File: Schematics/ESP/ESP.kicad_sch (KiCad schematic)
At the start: 28 parts, among them J1 Barrel_Jack, Q1 IRLB8721PBF, Q10 IRLML0030, Q11 IRLML0030, Q12 IRLML0030, Q13 IRLML0030, Q14 IRLML0030, Q2 IRLB8721PBF, Q3 IRLB8721PBF, Q4 IRLB8721PBF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

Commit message: small tweaks
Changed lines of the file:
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@@
+    (stroke (width 0) (type default))
+  )
+  (wire (pts (xy 199.39 114.3) (xy 199.39 107.95))
     (stroke (width 0) (type default))
   )
@@
     (stroke (width 0) (type default))
   )
+  (wire (pts (xy 200.66 35.56) (xy 200.66 43.18))
+    (stroke (width 0) (type default))
+  )
   (wire (pts (xy 95.25 106.68) (xy 95.25 123.19))
     (stroke (width 0) (type default))
@@
   )
   (wire (pts (xy 69.85 63.5) (xy 95.25 63.5))
+    (stroke (width 0) (type default))
+  )
+  (wire (pts (xy 229.87 120.65) (xy 233.68 120.65))
     (stroke (width 0) (type default))
   )
@@
     )
   )
+  (global_label "Regulated 5V" (shape output) (at 233.68 120.65 0) (fields_autoplaced)
+    (effects (font (size 1.27 1.27)) (justify left))
+    (property "Intersheetrefs" "${INTERSHEET_REFS}" (at 249.08 120.65 0)
+      (effects (font (size 1.27 1.27)) (justify left) hide)
+    )
+  )
+  (global_label "Regulated 5V" (shape input) (at 200.66 35.56 90) (fields_autoplaced)
+    (effects (font (size 1.27 1.27)) (justify left))
+    (property "Intersheetrefs" "${INTERSHEET_REFS}" (at 200.66 20.16 90)
+      (effects (font (size 1.27 1.27)) (justify left) hide)
+    )
+  )
   (global_label "P-" (shape input) (at 259.08 27.94 180) (fields_autoplaced)
     (effects (font (size 1.27 1.27)) (justify right))
@@
     )
   )
+  (global_label "Power Supply" (shape input) (at 199.39 107.95 90) (fields_autoplaced)
+    (effects (font (size 1.27 1.27)) (justify left))
+    (property "Intersheetrefs" "${INTERSHEET_REFS}" (at 199.3106 92.6555 90)
+      (effects (font (size 1.27 1.27)) (justify left) hide)
+    )
+  )

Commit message: Schematics
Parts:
- removed BT1, BT2, BT4: Battery_Cell, symbol Device:Battery_Cell
- removed Q1, Q2, Q3, Q4, Q7, Q8: IRLB8721PBF, Package_TO_SOT_THT:TO-220-3_Vertical, symbol Transistor_FET:IRLB8721PBF
- removed Q10, Q11, Q12, Q13, Q14, Q9: IRLML0030, Package_TO_SOT_SMD:SOT-23, symbol Transistor_FET:IRLML0030
- added R11, R9: 2.7k, Resistor_SMD:R_1206_3216Metric_Pad1.30x1.75mm_HandSolder, symbol Device:R
- added SW2: SW_Push, Button_Switch_SMD:SW_SPST_PTS645, symbol Switch:SW_Push
- added U8, U9: 74LVC1G11, Package_TO_SOT_SMD:SOT-23-6_Handsoldering, symbol 74xGxx:74LVC1G11
- C1, C2, C3: footprint (none) -> Capacitor_Tantalum_SMD:CP_EIA-7343-31_Kemet-D_Pad2.25x2.55mm_HandSolder
- J1: footprint (none) -> RAPC722X:SWITCHCRAFT_RAPC722X
- Q6: digikey link (none) -> https://www.digikey.fi/en/products/detail/infineon-technolo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
- R2, R3, R5, R6: footprint (none) -> Resistor_SMD:R_1206_3216Metric_Pad1.30x1.75mm_HandSolder
- U2: digikey link (none) -> https://www.digikey.fi/en/products/detail/diodes-incorporat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
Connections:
- net P-: now also Q5.3 (S), SW2.1; no longer Q6.3 (S), R5.1
- net at Q6.1 (G): now also U9.4
- net DO2: now reaches U1.4 (DO)
- net DO2: now also U9.1
- net Cell2+: now reaches C2.1, R2.2, U2.3 (VSS)
- net Cell2+: now also R11.1; no longer U2.1 (VM)
- net Cell1+: now reaches C1.1, R6.2, U1.3 (VSS)
- net Cell1+: now also R9.1; no longer Q5.1 (G), U1.1 (VM)
- net DO1: now reaches U2.4 (DO)
- net DO1: now also U9.6
- net at C2.2, U2.2 (VDD): now also R3.2; no longer R3.1
- net CO2: now reaches U1.5 (CO)
- net CO2: now also U8.1
- net Battery-: now reaches C3.1, U3.3 (VSS)
- net Battery-: now also Q6.3 (S), R5.1, SW2.2; no longer Q5.3 (S)
- net at C3.2, R6.1, U3.2 (VDD): now also U8.5 (VCC), U9.5 (VCC)
- net DO3: now reaches U3.4 (DO)
- net DO3: now also U9.3
- net CO1: now reaches U2.5 (CO)
- net CO1: now also U8.6
- net CO3: now reaches U3.5 (CO)
- net CO3: now also U8.3
- net P+ renamed Battery+
- net Battery+: now also R3.1; no longer R3.2
- new net: R9.2, U1.1 (VM)
- new net: Q5.1 (G), U8.4
- new net: R11.2, U2.1 (VM)
- new net GND: U8.2 (GND), U9.2 (GND)
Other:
- note added: "CO/DO pins are high when battery voltage is within allowed range, thus a´ctivating their respective switches. when all the switches are activated, the final two MOSFETs are activated adn the negative terminal of the battery is connected to the negative terminal of the circuit"
- note added: "Capacitor and resistor to stabilize input voltage, recommmeneded values are: 330 Ohm and 100nF"
- note added: "Important note: To kickstart the circuit, the negative battery terminal needs to be shorted to the negative charger terminal using this switch"
- note added: "current sense resistor, value recommended by datatsheet 2.7K"
- moved on the sheet: C1, C2, C3, J1, Q5, Q6, R2, R5, R6, U1, U2, U3

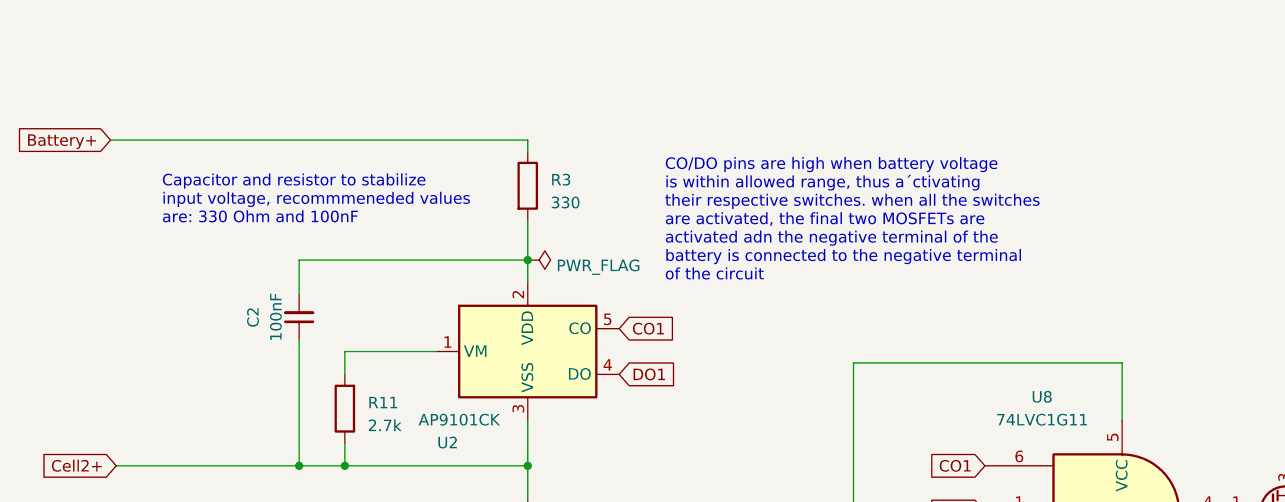
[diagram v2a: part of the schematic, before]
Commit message: Added footprints, IR pins and bill of materials-Khalil
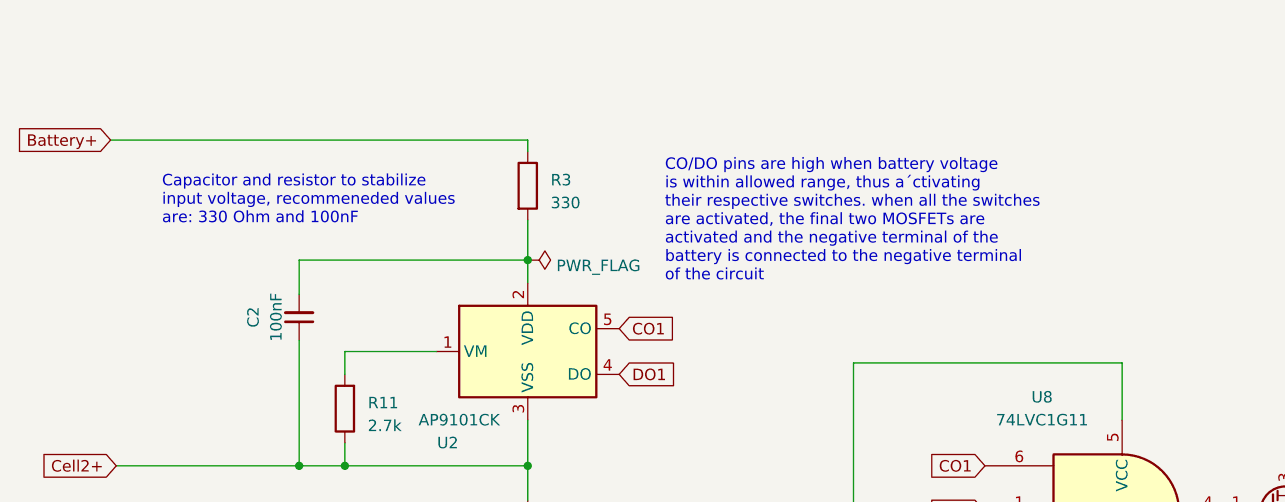
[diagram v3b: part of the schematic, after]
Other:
- note added: "CO/DO pins are high when battery voltage is within allowed range, thus a´ctivating their respective switches. when all the switches are activated, the final two MOSFETs are activated and the negative terminal of the battery is connected to the negative terminal of the circuit"
- note added: "Capacitor and resistor to stabilize input voltage, recommeneded values are: 330 Ohm and 100nF"
- note removed: "CO/DO pins are high when battery voltage is within allowed range, thus a´ctivating their respective switches. when all the switches are activated, the final two MOSFETs are activated adn the negative terminal of the battery is connected to the negative terminal of the circuit"
- note removed: "Capacitor and resistor to stabilize input voltage, recommmeneded values are: 330 Ohm and 100nF"
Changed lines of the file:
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@@
     (stroke (width 0) (type default))
   )
-  (text "CO/DO pins are high when battery voltage\nis within allowed range, thus a´ctivating\ntheir respective switches. when all the switches\nare activated, the final two MOSFETs are\nactivated adn the negative terminal of the\nbattery is connected to the negative terminal\nof the circuit"
+  (text "CO/DO pins are high when battery voltage\nis within allowed range, thus a´ctivating\ntheir respective switches. when all the switches\nare activated, the final two MOSFETs are\nactivated and the negative terminal of the\nbattery is connected to the negative terminal\nof the circuit"
     (at 107.95 50.8 0)
     (effects (font (size 1.27 1.27)) (justify left bottom))
   )
-  (text "Capacitor and resistor to stabilize\ninput voltage, recommmeneded values\nare: 330 Ohm and 100nF"
+  (text "Capacitor and resistor to stabilize\ninput voltage, recommeneded values\nare: 330 Ohm and 100nF"
     (at 52.07 44.45 0)
     (effects (font (size 1.27 1.27)) (justify left bottom))

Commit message: newer BOM
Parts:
- C1, C2, C3: Price (none) -> 0,63; digikey link (none) -> https://www.digikey.fi/en/products/detail/kemet/T491A104K03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
- J1: Price (none) -> 0,87; digikey link (none) -> https://www.digikey.fi/fi/products/detail/gct/DCJ200-10-A-K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
- Q5: Price (none) -> 1,33; digikey link (none) -> https://www.digikey.fi/en/products/detail/infineon-technolo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
- Q6: Price (none) -> 1,33
- R11, R5, R9: Price (none) -> 0,11; digikey link (none) -> https://www.digikey.fi/en/products/detail/yageo/RC0402FR-13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
- R2, R3, R6: Price (none) -> 0,11; digikey link (none) -> https://www.digikey.fi/en/products/detail/walsin-technology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
- SW2: Price (none) -> 0,3
- U1, U3: Price (none) -> 0,52; digikey link (none) -> https://www.digikey.fi/en/products/detail/diodes-incorporat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
- U2: Price (none) -> 0,52
- U8, U9: Price (none) -> 0,45
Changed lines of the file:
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@@
+      (effects (font (size 1.27 1.27)) hide)
+    )
+    (property "digikey link" "https://www.digikey.fi/en/products/detail/kemet/T491A104K035AT/818537" (at 67.31 54.61 0)
+      (effects (font (size 1.27 1.27)) hide)
+    )
+    (property "Price" "0,63" (at 67.31 54.61 0)
       (effects (font (size 1.27 1.27)) hide)
     )
@@
     )
     (property "Datasheet" "https://www.diodes.com/assets/Datasheets/AP9101C.pdf" (at 92.71 95.25 0)
+      (effects (font (size 1.27 1.27)) hide)
+    )
+    (property "digikey link" "https://www.digikey.fi/en/products/detail/diodes-incorporated/AP9101CK-AHTRG1/5731842" (at 92.71 96.52 0)
+      (effects (font (size 1.27 1.27)) hide)
+    )
+    (property "Price" "0,52" (at 92.71 96.52 0)
       (effects (font (size 1.27 1.27)) hide)
     )
@@
       (effects (font (size 1.27 1.27)) hide)
     )
+    (property "digikey link" "https://www.digikey.fi/fi/products/detail/gct/DCJ200-10-A-K1-K/9859579" (at 22.86 190.5 0)
+      (effects (font (size 1.27 1.27)) hide)
+    )
+    (property "Price" "0,87" (at 22.86 190.5 0)
+      (effects (font (size 1.27 1.27)) hide)
+    )
     (pin "1")
     (pin "2")
@@
       (effects (font (size 1.27 1.27)) (justify left) hide)
     )
+    (property "digikey link" "https://www.digikey.fi/en/products/detail/infineon-technologies/IRLB8721PBF/2127670?s=N4IgTCBcDaIJICUAyAhAHAdjARgAooDEQBdAXyA" (at 175.26 76.2 0)
+      (effects (font (size 1.27 1.27)) hide)
+    )
+    (property "Price" "1,33" (at 175.26 76.2 0)
+      (effects (font (size 1.27 1.27)) hide)
+    )
     (pin "1")
     (pin "2")
@@
     )
     (property "digikey link" "https://www.digikey.fi/en/products/detail/infineon-technologies/IRLB8721PBF/2127670?s=N4IgTCBcDaIJICUAyAhAHAdjARgAooDEQBdAXyA" (at 175.26 101.6 0)
+      (effects (font (size 1.27 1.27)) hide)
+    )
+    (property "Price" "1,33" (at 175.26 101.6 0)
       (effects (font (size 1.27 1.27)) hide)
     )
@@
       (effects (font (size 1.27 1.27)) hide)
     )
+    (property "Price" "0,3" (at 189.23 86.995 0)
+      (effects (font (size 1.27 1.27)) hide)
+    )
     (pin "1")
     (pin "2")
@@
       (effects (font (size 1.27 1.27)) hide)
     )
+    (property "digikey link" "https://www.digikey.fi/en/products/detail/walsin-technology-corporation/WR04X331-JTL/13240790" (at 92.71 120.65 0)
+      (effects (font (size 1.27 1.27)) hide)
+    )
+    (property "Price" "0,11" (at 92.71 120.65 0)
+      (effects (font (size 1.27 1.27)) hide)
+    )
     (pin "1")
     (pin "2")
@@
       (effects (font (size 1.27 1.27)) hide)
     )
+    (property "digikey link" "https://www.digikey.fi/en/products/detail/yageo/RC0402FR-132K7L/14286631" (at 72.39 64.77 0)
+      (effects (font (size 1.27 1.27)) hide)
+    )
+    (property "Price" "0,11" (at 72.39 64.77 0)
+      (effects (font (size 1.27 1.27)) hide)
+    )
     (pin "1")
     (pin "2")
@@
     )
     (property "Datasheet" "~" (at 72.39 104.14 0)
+      (effects (font (size 1.27 1.27)) hide)
+    )
+    (property "digikey link" "https://www.digikey.fi/en/products/detail/yageo/RC0402FR-132K7L/14286631" (at 72.39 104.14 0)
+      (effects (font (size 1.27 1.27)) hide)
+    )
+    (property "Price" "0,11" (at 72.39 104.14 0)
       (effects (font (size 1.27 1.27)) hide)
     )
@@
       (effects (font (size 1.27 1.27)) hide)
     )
+    (property "digikey link" "https://www.digikey.fi/en/products/detail/walsin-technology-corporation/WR04X331-JTL/13240790" (at 92.71 78.74 0)
+      (effects (font (size 1.27 1.27)) hide)
+    )
+    (property "Price" "0,11" (at 92.71 78.74 0)
+      (effects (font (size 1.27 1.27)) hide)
+    )
     (pin "1")
     (pin "2")
@@
       (effects (font (size 1.27 1.27)) hide)
     )
+    (property "digikey link" "https://www.digikey.fi/en/products/detail/kemet/T491A104K035AT/818537" (at 67.31 138.43 0)
+      (effects (font (size 1.27 1.27)) hide)
+    )
+    (property "Price" "0,63" (at 67.31 138.43 0)
+      (effects (font (size 1.27 1.27)) hide)
+    )
     (pin "1")
     (pin "2")
@@
     )
     (property "Datasheet" "https://www.diodes.com/assets/Datasheets/AP9101C.pdf" (at 92.71 137.16 0)
+      (effects (font (size 1.27 1.27)) hide)
+    )
+    (property "digikey link" "https://www.digikey.fi/en/products/detail/diodes-incorporated/AP9101CK-AHTRG1/5731842" (at 92.71 138.43 0)
+      (effects (font (size 1.27 1.27)) hide)
+    )
+    (property "Price" "0,52" (at 92.71 138.43 0)
       (effects (font (size 1.27 1.27)) hide)
     )
@@
       (effects (font (size 1.27 1.27)) hide)
     )
+    (property "digikey link" "https://www.digikey.fi/en/products/detail/yageo/RC0402FR-132K7L/14286631" (at 72.39 145.415 0)
+      (effects (font (size 1.27 1.27)) hide)
+    )
+    (property "Price" "0,11" (at 72.39 145.415 0)
+      (effects (font (size 1.27 1.27)) hide)
+    )
     (pin "1")
     (pin "2")
@@
     )
     (property "digikey link" "https://www.digikey.fi/en/products/detail/diodes-incorporated/74LVC1G11W6-7/3829446" (at 158.75 76.2 0)
+      (effects (font (size 1.27 1.27)) hide)
+    )
+    (property "Price" "0,45" (at 158.75 76.2 0)
       (effects (font (size 1.27 1.27)) hide)
     )
@@
       (effects (font (size 1.27 1.27)) hide)
     )
+    (property "Price" "0,45" (at 158.75 101.6 0)
+      (effects (font (size 1.27 1.27)) hide)
+    )
     (pin "1")
     (pin "2")
@@
       (effects (font (size 1.27 1.27)) hide)
     )
+    (property "Price" "0,52" (at 92.71 58.42 0)
+      (effects (font (size 1.27 1.27)) hide)
+    )
     (pin "1")
     (pin "2")
@@
       (effects (font (size 1.27 1.27)) hide)
     )
+    (property "digikey link" "https://www.digikey.fi/en/products/detail/walsin-technology-corporation/WR04X331-JTL/13240790" (at 92.71 40.005 0)
+      (effects (font (size 1.27 1.27)) hide)
+    )
+    (property "Price" "0,11" (at 92.71 40.005 0)
+      (effects (font (size 1.27 1.27)) hide)
+    )
     (pin "1")
     (pin "2")
@@
       (effects (font (size 1.27 1.27)) hide)
     )
+    (property "digikey link" "https://www.digikey.fi/en/products/detail/kemet/T491A104K035AT/818537" (at 66.04 95.25 0)
+      (effects (font (size 1.27 1.27)) hide)
+    )
+    (property "Price" "0,63" (at 66.04 95.25 0)
+      (effects (font (size 1.27 1.27)) hide)
+    )

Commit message: Can Pull
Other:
- note added: "Battery charger sheet"
- company: (none) -> ESP project
- title: (none) -> Vaccuum cleaner Robot
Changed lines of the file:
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@@
 (kicad_sch (version 20230121) (generator eeschema)
   (paper "A4")
+  (title_block
+    (title "Vaccuum cleaner Robot")
+    (date "2023-03-18")
+    (rev "Version 0.0.1")
+    (company "ESP project")
+  )
   (junction (at 92.71 110.49) (diameter 0) (color 0 0 0 0)
   )
@@
     (effects (font (size 1.27 1.27)) (justify left bottom))
   )
+  (text "Battery charger sheet" (at 17.78 20.32 0)
+    (effects (font (size 4 4) (thickness 0.8) bold) (justify left bottom))
+  )
   (text "Capacitor and resistor to stabilize\ninput voltage, recommeneded values\nare: 330 Ohm and 100nF"

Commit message: fixed BOM
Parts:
- C1, C2, C3: footprint Capacitor_Tantalum_SMD:CP_EIA-7343-31_Kemet-D_Pad2.25x2.55mm_HandSolder -> Capacitor_SMD:C_1206_3216Metric_Pad1.33x1.80mm_HandSolder
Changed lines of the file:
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@@
       (effects (font (size 1.27 1.27)))
     )
-    (property "Footprint" "Capacitor_Tantalum_SMD:CP_EIA-7343-31_Kemet-D_Pad2.25x2.55mm_HandSolder" (at 67.31 54.61 0)
+    (property "Footprint" "Capacitor_SMD:C_1206_3216Metric_Pad1.33x1.80mm_HandSolder" (at 67.31 54.61 0)
       (effects (font (size 1.27 1.27)) hide)
     )
@@
       (effects (font (size 1.27 1.27)))
     )
-    (property "Footprint" "Capacitor_Tantalum_SMD:CP_EIA-7343-31_Kemet-D_Pad2.25x2.55mm_HandSolder" (at 67.31 138.43 0)
+    (property "Footprint" "Capacitor_SMD:C_1206_3216Metric_Pad1.33x1.80mm_HandSolder" (at 67.31 138.43 0)
       (effects (font (size 1.27 1.27)) hide)
     )
@@
       (effects (font (size 1.27 1.27)))
     )
-    (property "Footprint" "Capacitor_Tantalum_SMD:CP_EIA-7343-31_Kemet-D_Pad2.25x2.55mm_HandSolder" (at 66.04 95.25 0)
-      (effects (font (size 1.27 1.27)) hide)
-    )
+    (property "Footprint" "Capacitor_SMD:C_1206_3216Metric_Pad1.33x1.80mm_HandSolder" (at 66.04 95.25 0)
+      (effects (font (size 1.27 1.27)) hide)
+    )
